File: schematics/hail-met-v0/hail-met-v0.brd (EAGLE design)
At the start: 100 x 80 mm, 87 parts, among them IC1 MCP73871, U1 ATMEGA328P, U2 TLC5917ID, Y1 16MHZ

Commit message: updated schematic with pins (CPU pins not verified)
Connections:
- net N$30 renamed CHG_STAT
- net N$38 renamed BT_CONN
- net N$40 renamed BT_PAIR
- removed net BTH_CMD: U$3.GPIO9, U1.1
- removed net BTH_EVENT: U$3.GPIO2, U1.32
- removed net N$14: U2.4
- removed net N$28: U1.24
- removed net N$29: U1.25
- removed net N$39: U1.10
- removed net N$41: U1.12
- removed net N$42: U1.14
- removed net N$44: U1.16
- new net BT_CMD: U$3.GPIO9, U1.14
- new net BT_DISC: U1.2
- new net BT_EVENT: U$3.GPIO2, U1.12
- new net LED_LE: U1.16, U2.4
- new net SIG_LEFT: U1.32
- new net SIG_RIGHT: U1.1
- net CHG_DONE: now also U1.25
- net CHG_PWR: now also U1.24
- net DEV_EN: now also U1.13; no longer U1.2
- net GND: now also ATM_PWR.4
- net LED_OE: now also U1.10; no longer U1.13
- net N$32: no longer ATM_PWR.4
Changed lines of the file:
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@@
 <contactref element="C7" pad="2"/>
 <contactref element="C8" pad="2"/>
-<contactref element="R1" pad="2"/>
 <contactref element="U$2" pad="GND"/>
 <contactref element="U$3" pad="GND0"/>
@@
 <contactref element="R12" pad="2"/>
 <contactref element="MPU-6050" pad="8"/>
+<contactref element="ATM_PWR" pad="4"/>
+<contactref element="R1" pad="2"/>
 <wire x1="-144.78" y1="-93.98" x2="-144.78" y2="-101.6" width="0" layer="19" extent="1-1"/>
 <wire x1="-144.78" y1="-86.36" x2="-144.78" y2="-93.98" width="0" layer="19" extent="1-1"/>
@@
 <wire x1="-25.94" y1="53.61" x2="-26.94" y2="52.61" width="0" layer="19" extent="1-1"/>
 <wire x1="-26.67" y1="68.58" x2="-25.94" y2="53.61" width="0" layer="19" extent="1-1"/>
+<wire x1="-25.4" y1="73.533" x2="-26.67" y2="68.58" width="0" layer="19" extent="1-1"/>
+<wire x1="-27.57" y1="80.01" x2="-25.4" y2="73.533" width="0" layer="19" extent="1-1"/>
+<wire x1="-35.19" y1="80.01" x2="-27.57" y2="80.01" width="0" layer="19" extent="1-1"/>
+<wire x1="-39" y1="80.01" x2="-35.19" y2="80.01" width="0" layer="19" extent="1-1"/>
 <wire x1="-35.56" y1="68.58" x2="-26.67" y2="68.58" width="0" layer="19" extent="1-1"/>
-<wire x1="-35.19" y1="80.01" x2="-35.56" y2="68.58" width="0" layer="19" extent="1-1"/>
-<wire x1="-39" y1="80.01" x2="-35.19" y2="80.01" width="0" layer="19" extent="1-1"/>
-<wire x1="-27.57" y1="80.01" x2="-35.19" y2="80.01" width="0" layer="19" extent="1-1"/>
 <wire x1="-50.43" y1="80.01" x2="-39" y2="80.01" width="0" layer="19" extent="1-1"/>
 <wire x1="-56.25" y1="78.74" x2="-50.43" y2="80.01" width="0" layer="19" extent="1-1"/>
@@
 <wire x1="-75.3" y1="74.93" x2="-68.58" y2="74.93" width="0" layer="19" extent="1-1"/>
 <wire x1="-60.96" y1="66.04" x2="-58.69" y2="74.93" width="0" layer="19" extent="1-1"/>
-<wire x1="-14.34" y1="80.01" x2="-27.57" y2="80.01" width="0" layer="19" extent="1-1"/>
+<wire x1="-14.34" y1="80.01" x2="-25.4" y2="73.533" width="0" layer="19" extent="1-1"/>
 </signal>
 <signal name="VIN">
@@
 <signal name="LED_OE">
 <contactref element="U2" pad="13"/>
-<contactref element="U1" pad="13"/>
-<wire x1="-17.38" y1="37.6174" x2="-49.53" y2="10.16" width="0" layer="19" extent="1-1"/>
-</signal>
-<signal name="N$14">
+<contactref element="U1" pad="10"/>
+<wire x1="-19.78" y1="37.6174" x2="-49.53" y2="10.16" width="0" layer="19" extent="1-1"/>
+</signal>
+<signal name="LED_LE">
 <contactref element="U2" pad="4"/>
+<contactref element="U1" pad="16"/>
+<wire x1="-14.98" y1="37.6174" x2="-54.3306" y2="10.16" width="0" layer="19" extent="1-1"/>
 </signal>
 <signal name="LED_CLK">
@@
 <contactref element="IC1" pad="6"/>
 <contactref element="R26" pad="2"/>
+<contactref element="U1" pad="24"/>
 <wire x1="-28.94" y1="52.61" x2="-147.69" y2="-80.01" width="0" layer="19" extent="1-1"/>
+<wire x1="-13.4874" y1="44.71" x2="-28.94" y2="52.61" width="0" layer="19" extent="1-1"/>
 <wire x1="-43.18" y1="69.63" x2="-28.94" y2="52.61" width="0" layer="19" extent="1-1"/>
 </signal>
@@
 <contactref element="DONE" pad="C"/>
 <contactref element="R25" pad="2"/>
+<contactref element="U1" pad="25"/>
 <wire x1="-28.44" y1="52.61" x2="-143.88" y2="-80.01" width="0" layer="19" extent="1-1"/>
 <wire x1="-16.51" y1="51.85" x2="-28.44" y2="52.61" width="0" layer="19" extent="1-1"/>
+<wire x1="-14.98" y1="46.2026" x2="-16.51" y2="51.85" width="0" layer="19" extent="1-1"/>
 </signal>
 <signal name="CHG_STAT1">
@@
 <wire x1="-153.3" y1="-128.27" x2="-149.19" y2="-128.89" width="0" layer="19" extent="1-1"/>
 </signal>
-<signal name="N$28">
-<contactref element="U1" pad="24"/>
-</signal>
-<signal name="N$29">
-<contactref element="U1" pad="25"/>
-</signal>
-<signal name="N$30">
+<signal name="CHG_STAT">
 <contactref element="U1" pad="26"/>
 </signal>
@@
 <contactref element="U1" pad="22"/>
 </signal>
-<signal name="N$38">
+<signal name="BT_CONN">
 <contactref element="U1" pad="9"/>
 </signal>
-<signal name="N$39">
-<contactref element="U1" pad="10"/>
-</signal>
-<signal name="N$40">
+<signal name="BT_PAIR">
 <contactref element="U1" pad="11"/>
 </signal>
-<signal name="N$41">
+<signal name="BT_EVENT">
 <contactref element="U1" pad="12"/>
-</signal>
-<signal name="N$42">
+<contactref element="U$3" pad="GPIO2"/>
+<wire x1="-18.18" y1="37.6174" x2="-104.14" y2="25.15" width="0" layer="19" extent="1-1"/>
+</signal>
+<signal name="BT_CMD">
 <contactref element="U1" pad="14"/>
+<contactref element="U$3" pad="GPIO9"/>
+<wire x1="-16.58" y1="37.6174" x2="-104.14" y2="15.55" width="0" layer="19" extent="1-1"/>
 </signal>
 <signal name="LED_SDI">
@@
 <contactref element="U2" pad="2"/>
 <wire x1="-15.78" y1="37.6174" x2="-54.3306" y2="12.7" width="0" layer="19" extent="1-1"/>
-</signal>
-<signal name="N$44">
-<contactref element="U1" pad="16"/>
 </signal>
 <signal name="CTS">
@@
 </signal>
 <signal name="N$32">
-<contactref element="ATM_PWR" pad="4"/>
 <contactref element="ATM_PC" pad="4"/>
 <contactref element="ATM_PD" pad="4"/>
 <wire x1="-120.65" y1="-34.417" x2="-120.65" y2="-39.497" width="0" layer="19" extent="1-1"/>
-<wire x1="-25.4" y1="73.533" x2="-120.65" y2="-34.417" width="0" layer="19" extent="1-1"/>
 </signal>
 <signal name="N$43">
@@
 <wire x1="-122.82" y1="-12.7" x2="-129.27" y2="-48.26" width="0" layer="19" extent="1-1"/>
 </signal>
-<signal name="BTH_EVENT">
-<contactref element="U$3" pad="GPIO2"/>
-<contactref element="U1" pad="32"/>
-<wire x1="-20.58" y1="46.2026" x2="-104.14" y2="25.15" width="0" layer="19" extent="1-1"/>
-</signal>
-<signal name="BTH_CMD">
-<contactref element="U$3" pad="GPIO9"/>
-<contactref element="U1" pad="1"/>
-<wire x1="-22.0726" y1="44.71" x2="-104.14" y2="15.55" width="0" layer="19" extent="1-1"/>
-</signal>
 <signal name="MPU_INT">
 <contactref element="MPU-6050" pad="3"/>
@@
 <signal name="DEV_EN">
 <contactref element="U$3" pad="PWREN"/>
-<contactref element="U1" pad="2"/>
-<wire x1="-22.0726" y1="43.91" x2="-99.19" y2="6.35" width="0" layer="19" extent="1-1"/>
+<contactref element="U1" pad="13"/>
+<wire x1="-17.38" y1="37.6174" x2="-99.19" y2="6.35" width="0" layer="19" extent="1-1"/>
 </signal>
 <signal name="MPU_VIO">
 <contactref element="MPU-6050" pad="7"/>
 </signal>
+<signal name="SIG_LEFT">
+<contactref element="U1" pad="32"/>
+</signal>
+<signal name="SIG_RIGHT">
+<contactref element="U1" pad="1"/>
+</signal>
+<signal name="BT_DISC">
+<contactref element="U1" pad="2"/>
+</signal>
 </signals>

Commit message: modified schematic slightly and began board layout.
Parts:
- removed R15, R25, R26: 1K, SparkFun-Passives:0805
- added J1: AVR_SPI_PRG_6PTH, SparkFun-Connectors:2X3
- moved EXT_PWR_JACK 269.6 mm to (72.4, 31.8)
- moved R12 249.1 mm to (33.0, 38.1), turned to 180 degrees
- moved U$5 243.6 mm to (33.0, 34.3), turned to 270 degrees
- moved ATM_PD 228.4 mm to (95.2, 7.62), turned to 90 degrees
- moved ATM_PC 223.7 mm to (91.4, 7.62), turned to 90 degrees
- moved PWR_BUTTON 221.7 mm to (73.7, 12.7), turned to 270 degrees
- moved NTC_THERM 213.7 mm to (73.7, 16.5), turned to 90 degrees
- moved SW_TR 186.8 mm to (-12.7, 35.6)
- moved SW_BFF 186.8 mm to (-12.7, 27.9)
- moved SW_BRR 186.8 mm to (-12.7, 20.3)
- moved SW_BSEL 186.8 mm to (-12.7, 12.7)
- moved SW_TL 186.8 mm to (-12.7, 43.2)
- moved CO_R 168.4 mm to (11.4, 20.3), turned to 90 degrees
- moved MPU-6050 163.1 mm to (-3.81, 39.4), turned to 90 degrees
- moved CO_L 162.0 mm to (6.35, 20.3), turned to 90 degrees
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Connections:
- new net N$21: J1.2
- net 3.3V: no longer R13.2, R15.1, R25.1, R26.1, R5.2, R6.2
- net CHG_DONE: no longer R25.2
- net CHG_PWR: no longer R26.2
- net CHG_STAT1: no longer R15.2
- net CHG_VOUT: now also C7.1, U$1.3
- net GND: now also J1.6
- net LED_CLK: now also J1.3
- net LED_LE: now also J1.1
- net LED_SDI: now also J1.4
- net RESET: now also J1.5
- net VCHG: now also R13.2, R5.2, R6.2
- net VIN: no longer C7.1, U$1.3
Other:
- board size 100 x 80 mm -> 77.1 x 61 mm

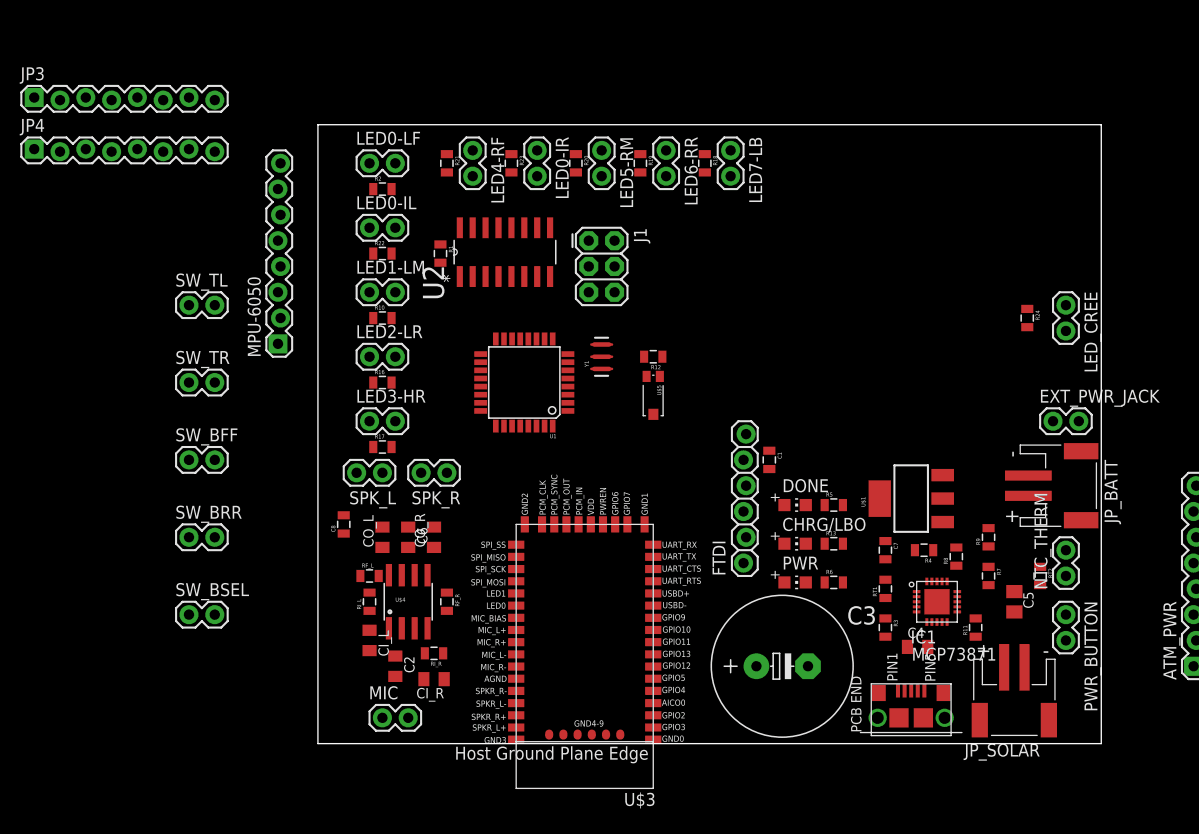
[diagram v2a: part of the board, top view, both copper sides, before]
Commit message: updated schematic/board and datasheets
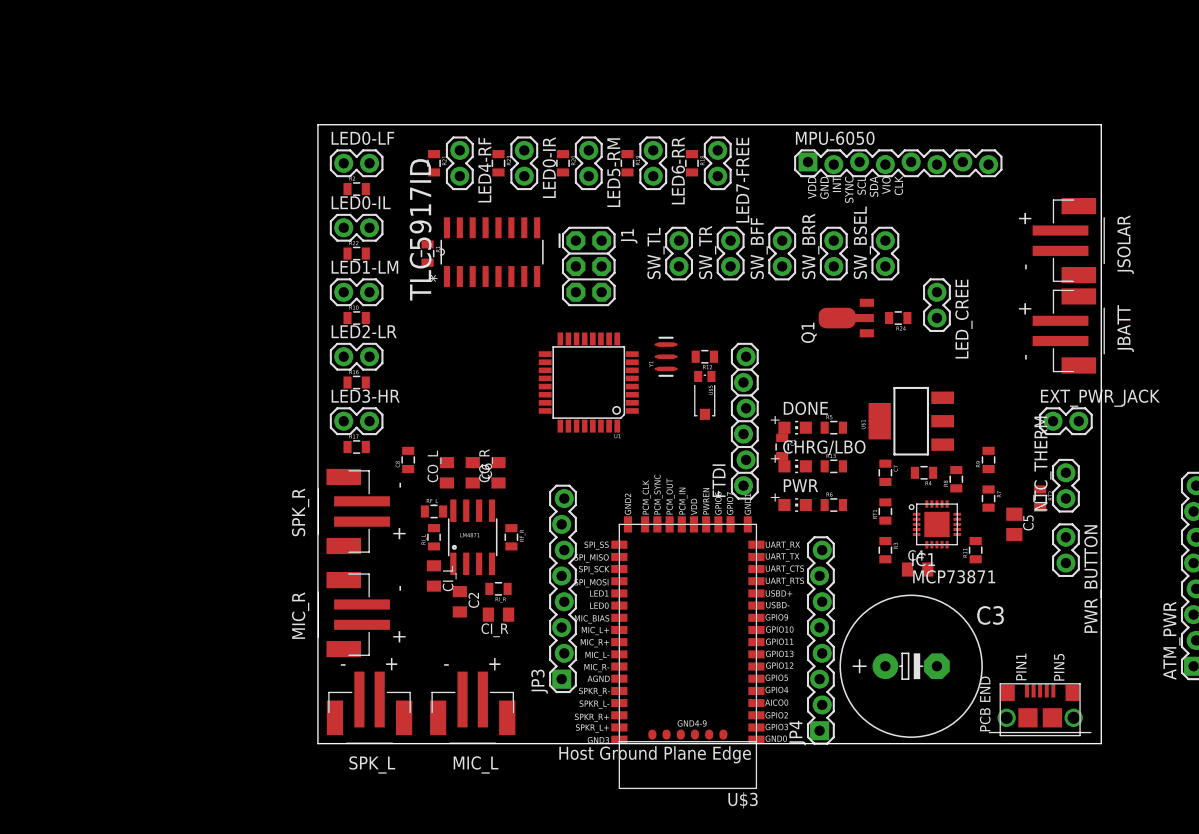
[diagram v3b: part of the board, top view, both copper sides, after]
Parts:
- removed JP_BATT, JP_SOLAR: (no value), adafruit:JST-PH-2-SMT-RA
- removed LED7-LB, MIC: M02PTH, SparkFun-Connectors:1X02
- removed U$4: LM4871, SparkFun:SO08
- removed U2: TLC5917ID, Texas Instruments_By_element14_Batch_1:SOIC127P600X175-16N
- added JBATT, JSOLAR, MIC_L, MIC_R: (no value), adafruit:JST-PH-2-SMT
- added LED7-FREE: M02PTH, SparkFun-Connectors:1X02
- added LM4871: LM4871, SparkFun:SO08
- added Q1: (no value), semicon-smd-ipc:SOT89
- added TLC5917ID: TLC5917ID, Texas Instruments_By_element14_Batch_1:SOIC127P600X175-16N
- R12: value (none) -> 10k
- SPK_L, SPK_R: value M02PTH -> (none); device SparkFun-Connectors:1X02 -> adafruit:JST-PH-2-SMT
- moved JP4 96.3 mm to (49.5, 1.27), turned to 90 degrees
- moved JP3 77.3 mm to (24.1, 6.35), turned to 90 degrees
- moved SW_BSEL 76.7 mm to (55.9, 47.0), turned to 90 degrees
- moved SW_BRR 68.9 mm to (50.8, 47.0), turned to 90 degrees
- moved SW_BFF 61.4 mm to (45.7, 47.0), turned to 90 degrees
- moved MPU-6050 55.0 mm to (48.3, 57.1), turned to 0 degrees
- moved SW_TR 54.6 mm to (40.6, 47.0), turned to 90 degrees
- moved SW_TL 48.4 mm to (35.6, 47.0), turned to 90 degrees
- moved SPK_L 24.2 mm to (5.08, 2.54)
- moved LED_CREE 12.8 mm to (61.0, 44.5)
- moved C3 12.7 mm to (58.4, 7.62)
- moved U$2 12.7 mm to (71.1, 2.54)
- moved R24 12.7 mm to (57.1, 41.9), turned to 180 degrees
- moved SPK_R 10.9 mm to (2.54, 22.9), turned to 90 degrees
- moved U$3 10.2 mm to (43.2, 21.6)
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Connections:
- net CHG_STAT renamed C
- removed net N$31: CO_L.2, SPK_L.1
- removed net N$33: U1.19
- removed net N$69: U$3.UART_TX
- removed net N$70: U$3.UART_RX
- removed net SIG_LEFT: U1.32
- removed net SIG_RIGHT: U1.1
- new net A: U1.24
- new net B: U1.25
- new net BT_GPIO10: JP4.8, U$3.GPIO10
- new net BT_GPIO2: JP4.1
- new net BT_GPIO3: JP4.2, U$3.GPIO3
- new net BT_GPIO4: JP4.3, U$3.GPIO4
- new net BT_GPIO5: JP4.4, U$3.GPIO5
- new net BT_GPIO6: JP4.5, U$3.GPIO6
- new net BT_GPIO7: JP4.6, U$3.GPIO7
- new net BT_GPIO9: JP4.7
- new net LED_CREE: Q1.1, U1.23
- new net N$14: CO_L.2, SPK_L.2
- new net N$19: Q1.2, R24.2
- net 3.3V: now also LED7-FREE.1, LM4871.6, TLC5917ID.16, U$3.VDD; no longer LED7-LB.1, LED_CREE.1, U$4.6, U2.16
- net AMB_IN: now also U1.19; no longer U1.23
- net CHG_DONE: no longer U1.25
- net CHG_PWR: no longer U1.24
- net GND: now also JBATT.1, JSOLAR.1, LM4871.1, LM4871.7, Q1.3, SPK_L.1, SPK_R.1, TLC5917ID.1; no longer JP_BATT.1, JP_SOLAR.1, SPK_L.2, SPK_R.2, U$4.7, U2.1
- net LED_CLK: now also TLC5917ID.3; no longer U2.3
- net LED_LE: now also TLC5917ID.4; no longer U2.4
- net LED_OE: now also TLC5917ID.13; no longer U2.13
- net LED_SDI: now also TLC5917ID.2; no longer U2.2
- net MIC_L+: now also MIC_L.2, U$3.MIC_L+; no longer JP4.8
- net MIC_L-: now also MIC_L.1, U$3.MIC_L-; no longer JP4.6
- net MIC_R+: now also MIC_R.2, U$3.MIC_R+; no longer JP4.7
- net MIC_R-: now also MIC_R.1, U$3.MIC_R-; no longer JP4.5
- net N$10: now also TLC5917ID.10; no longer U2.10
- net N$11: now also TLC5917ID.11; no longer U2.11
- net N$12: now also TLC5917ID.12; no longer U2.12
- net N$27: now also SPK_R.2; no longer SPK_R.1
- net N$5: now also TLC5917ID.5; no longer U2.5
- net N$56: now also TLC5917ID.15; no longer U2.15
- net N$6: now also TLC5917ID.6; no longer U2.6
- net N$61: now also LED7-FREE.2; no longer LED7-LB.2
- net N$7: now also TLC5917ID.7; no longer U2.7
- net N$71: now also LM4871.4; no longer U$4.4
- net N$74: now also LM4871.2; no longer U$4.2
- net N$75: now also LM4871.3; no longer U$4.3
- net N$8: now also TLC5917ID.8; no longer U2.8
- net N$80: now also JSOLAR.2; no longer JP_SOLAR.2
- net N$9: now also TLC5917ID.9; no longer U2.9
- net RXD: now also U$3.UART_TX
- net SPKR_L: now also LM4871.8; no longer U$4.8
- net SPKR_L+: no longer JP4.1
- net SPKR_L-: no longer JP4.3
- net SPKR_R: now also LM4871.5; no longer U$4.5
- net SPKR_R+: no longer JP4.2
- net SPKR_R-: no longer JP4.4
- net SW_TL: now also U1.32
- net SW_TR: now also U1.1
- net TXD: now also U$3.UART_RX
- net VBATT: now also JBATT.2; no longer JP_BATT.2
- net VCHG: now also LED_CREE.1
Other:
- board text added: "VDD GND INT SYNC SCL SDA VIO CLK"
